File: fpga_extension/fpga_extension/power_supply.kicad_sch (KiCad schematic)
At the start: 3 parts, among them U1 AMS1117-1.2

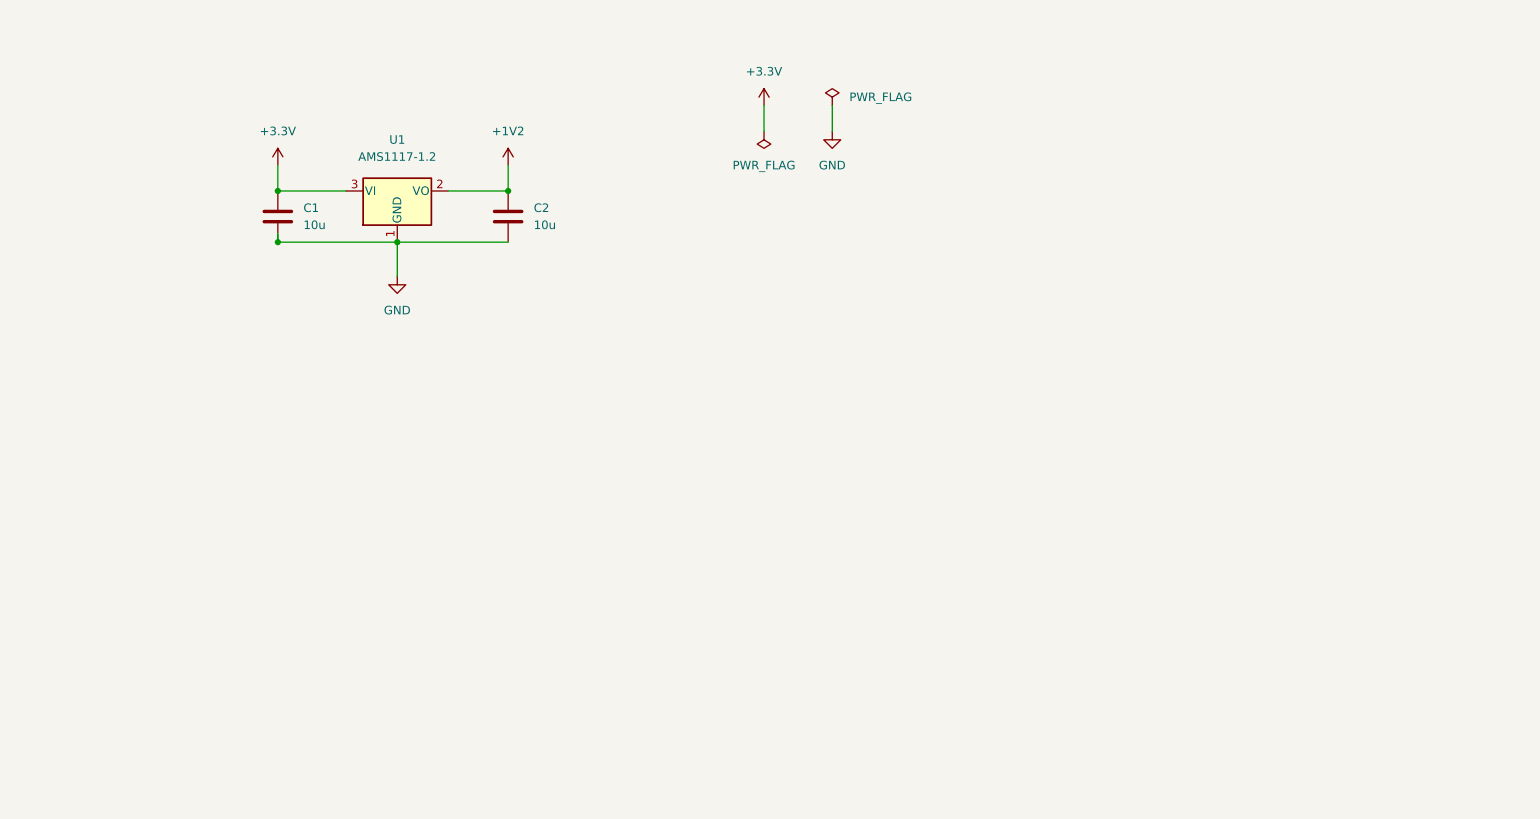
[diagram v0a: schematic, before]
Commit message: qspi added
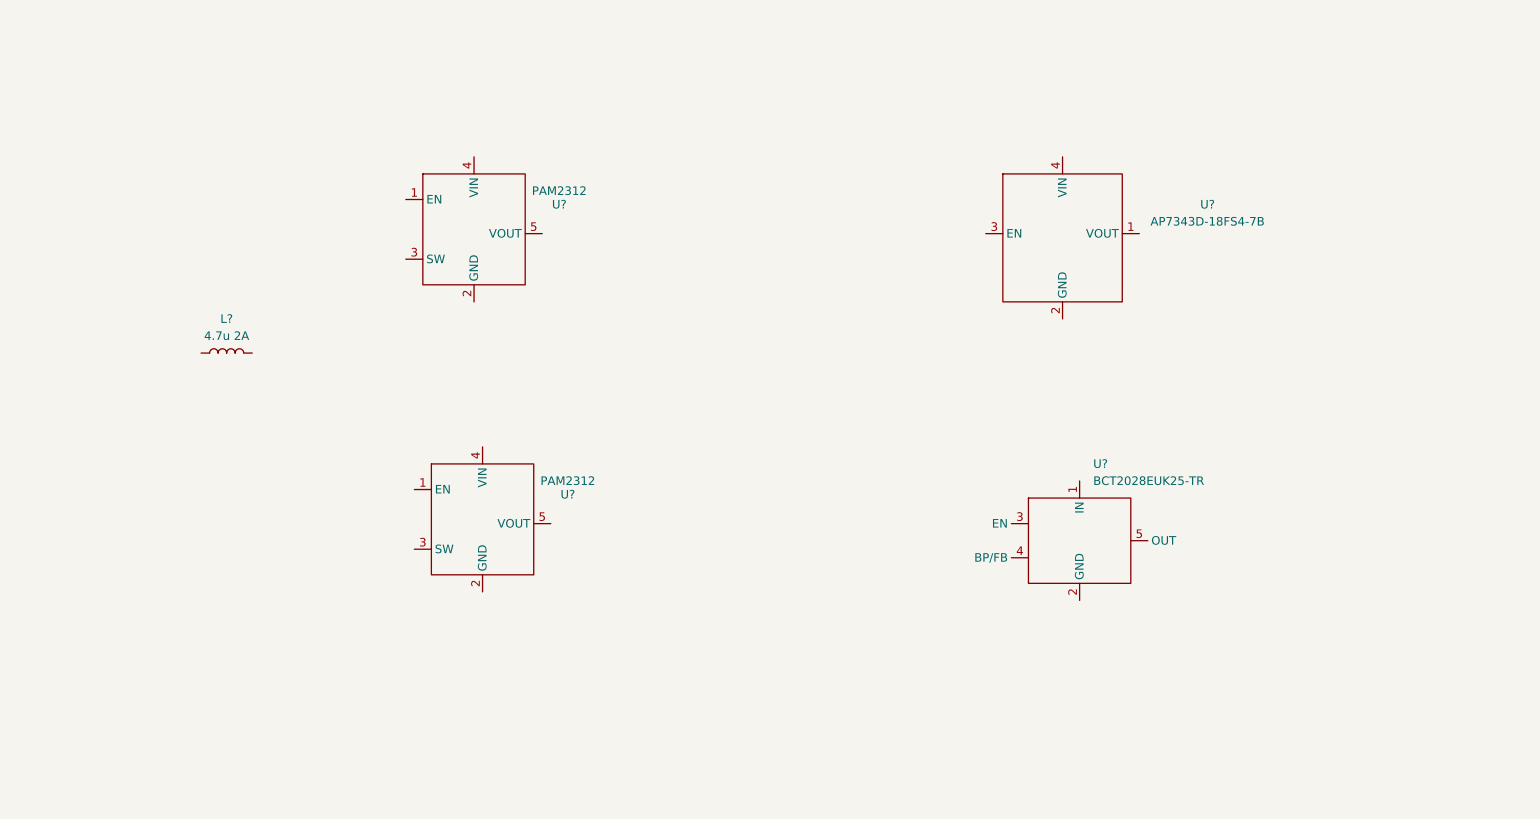
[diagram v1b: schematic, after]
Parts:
- removed C1, C2: 10u, Capacitor_SMD:C_0603_1608Metric_Pad1.08x0.95mm_HandSolder, symbol Device:C
- removed U1: AMS1117-1.2, Package_TO_SOT_SMD:SOT-223-3_TabPin2, symbol custom_ldo:AMS1117-1.2
- added L?: 4.7u 2A, fpga_extension:L_TDK_SLF6025, symbol Device:L
- added U? (x2): PAM2312, Package_TO_SOT_SMD:TSOT-23-5_HandSoldering, symbol fpga_extension_library:PAM2312
- added U?: BCT2028EUK25-TR, Package_TO_SOT_SMD:SOT-23-5_HandSoldering, symbol fpga_extension_library:BCT2028EUK25-TR
- added U?: AP7343D-18FS4-7B, fpga_extension:VREG_AP7340D-25FS4-7, symbol fpga_extension_library:AP7343D-18FS4-7B

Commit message: some ERC fixes
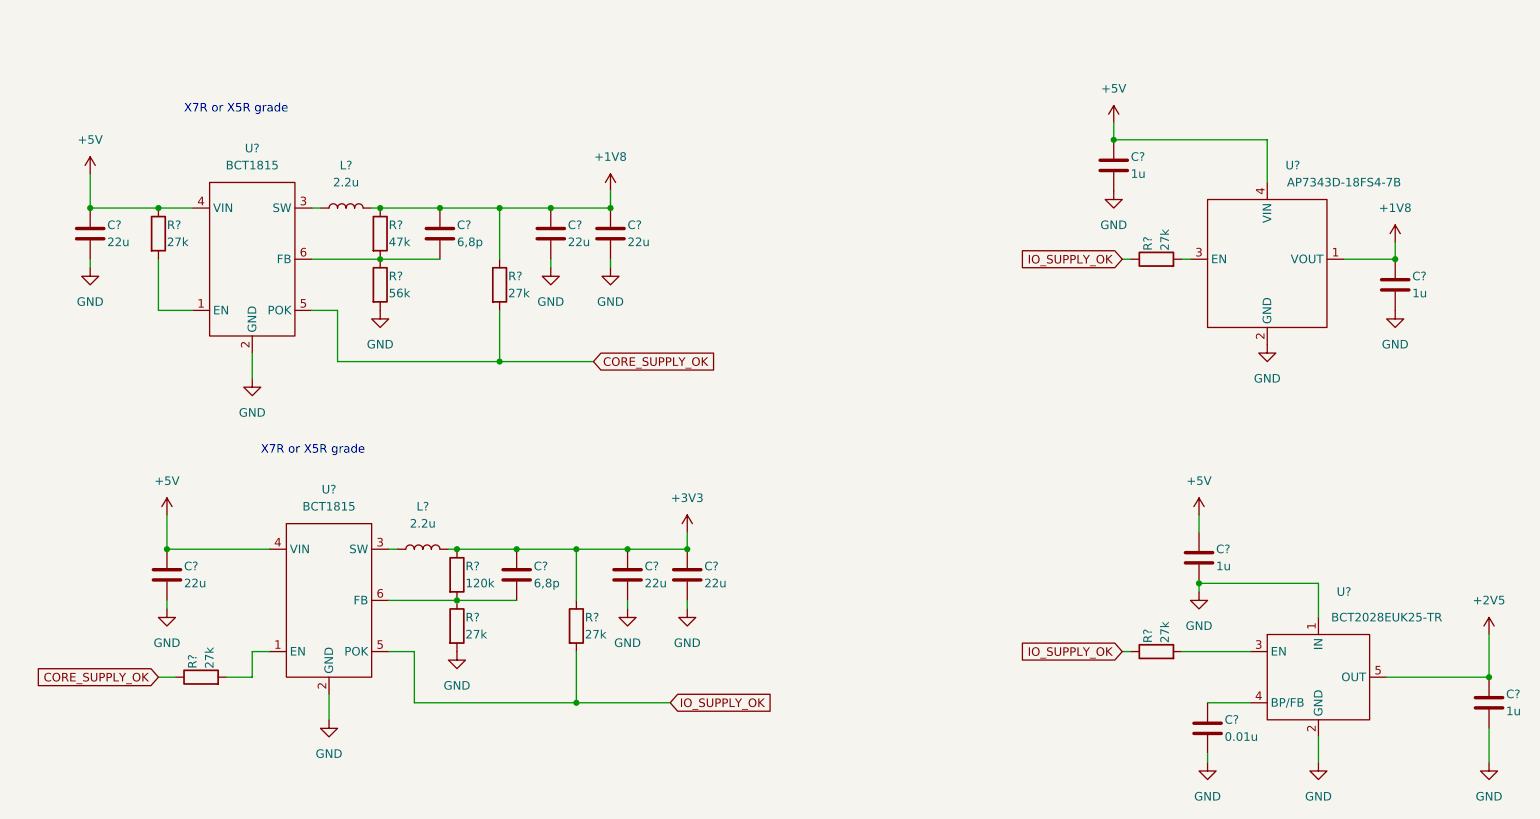
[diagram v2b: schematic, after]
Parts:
- removed L?: 4.7u 2A, fpga_extension:L_TDK_SLF6025, symbol Device:L
- removed U? (x2): PAM2312, Package_TO_SOT_SMD:TSOT-23-5_HandSoldering, symbol fpga_extension_library:PAM2312
- removed U?: BCT2028EUK25-TR, Package_TO_SOT_SMD:SOT-23-5_HandSoldering, symbol fpga_extension_library:BCT2028EUK25-TR
- added C? (x6): 22u, symbol Device:C
- added C? (x4): 1u, symbol Device:C
- added C? (x2): 6,8p, symbol Device:C
- added C?: 0.01u, symbol Device:C
- added L? (x2): 2.2u, symbol Device:L
- added R? (x7): 27k, symbol Device:R
- added R?: 120k, symbol Device:R
- added R?: 56k, symbol Device:R
- added R?: 47k, symbol Device:R
- added U? (x2): BCT1815, Package_TO_SOT_SMD:SOT-23-6_Handsoldering, symbol fpga_extension_library:BCT1815
- added U?: BCT2028EUK25-TR, Package_TO_SOT_SMD:SOT-23-5_HandSoldering, symbol fpga_extension_library:BCT2028EUK25-TR
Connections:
- net +1V8: now reaches U?.1 (VOUT)
- net +1V8: now also C?.1, C?.1, C?.1, C?.1, L?.2, R?.1, R?.1
- net GND: now reaches U?.2 (GND)
- net GND: now also C?.2, C?.2, C?.2, C?.2, C?.2, C?.2, C?.2, C?.2, C?.2, C?.2, C?.2, R?.2, R?.2, U?.1 (IN), U?.2 (GND), U?.2 (GND), U?.2 (GND)
- net at U?.3 (EN): now also R?.2
- net +5V: now reaches U?.4 (VIN)
- net +5V: now also C?.1, C?.1, C?.1, C?.1, R?.1, U?.4 (VIN), U?.4 (VIN)
- new net: R?.2, U?.1 (EN) (x2)
- new net: L?.1, U?.3 (SW) (x2)
- new net: C?.2, R?.1, R?.2, U?.6 (FB) (x2)
- new net: R?.2, U?.3 (EN)
- new net: C?.1, U?.4 (BP/FB)
- new net +2V5: C?.1, U?.5 (OUT)
- new net +3V3: C?.1, C?.1, C?.1, L?.2, R?.1, R?.1
- new net CORE_SUPPLY_OK: R?.1, R?.2, U?.5 (POK)
- new net IO_SUPPLY_OK: R?.1, R?.1, R?.2, U?.5 (POK)
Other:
- note added: "X7R or X5R grade"
- moved on the sheet: U?

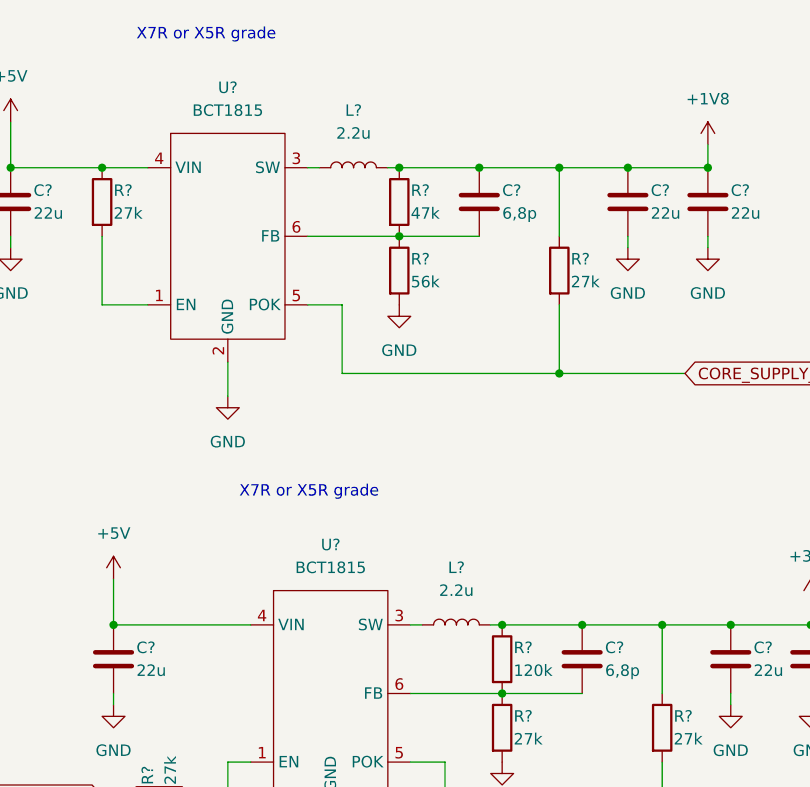
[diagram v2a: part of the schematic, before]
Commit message: gpu and motherboard passes tests, now time for fpga
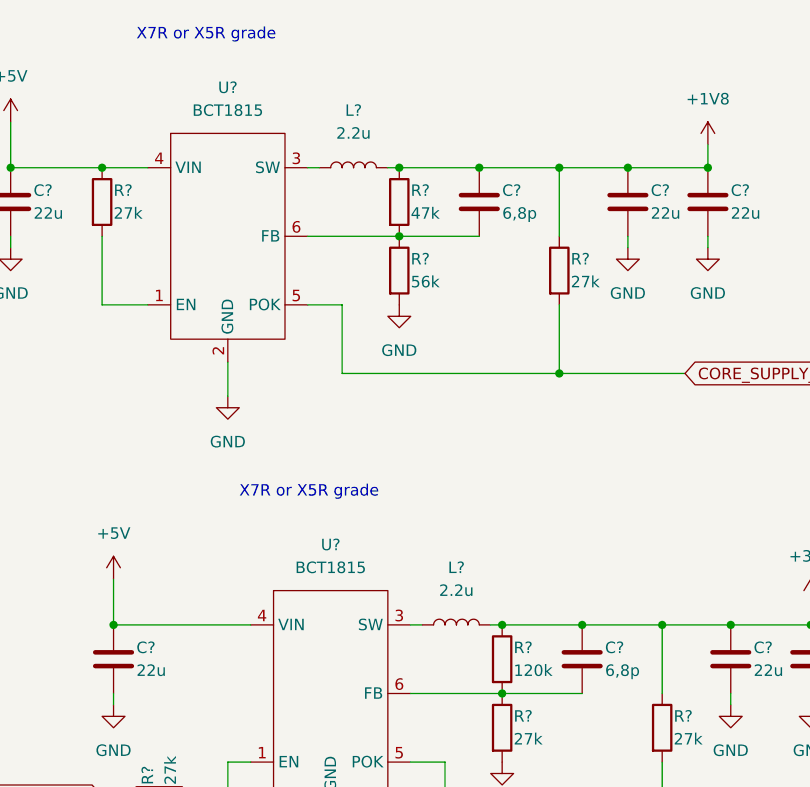
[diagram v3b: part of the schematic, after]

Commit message: refactored mainboard schematic
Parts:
- removed C? (x6): 22u, symbol Device:C
- removed C? (x4): 1u, symbol Device:C
- removed C? (x2): 6,8p, symbol Device:C
- removed C?: 0.01u, symbol Device:C
- removed L? (x2): 2.2u, symbol Device:L
- removed R? (x7): 27k, symbol Device:R
- removed R?: 120k, symbol Device:R
- removed R?: 56k, symbol Device:R
- removed R?: 47k, symbol Device:R
- removed U? (x2): BCT1815, Package_TO_SOT_SMD:SOT-23-6_Handsoldering, symbol fpga_extension_library:BCT1815
- removed U?: BCT2028EUK25-TR, Package_TO_SOT_SMD:SOT-23-5_HandSoldering, symbol fpga_extension_library:BCT2028EUK25-TR
- removed U?: AP7343D-18FS4-7B, fpga_extension:VREG_AP7340D-25FS4-7, symbol fpga_extension_library:AP7343D-18FS4-7B
- added C306, C308: 10u, Capacitor_SMD:C_0805_2012Metric_Pad1.18x1.45mm_HandSolder, symbol Device:C
- added C307: 4.7u, Capacitor_SMD:C_0805_2012Metric_Pad1.18x1.45mm_HandSolder, symbol Device:C
- added C310, C316: 100n, Capacitor_SMD:C_0603_1608Metric_Pad1.08x0.95mm_HandSolder, symbol Device:C
- added C313: 1u, Capacitor_SMD:C_0603_1608Metric_Pad1.08x0.95mm_HandSolder, symbol Device:C
- added C314: 3300p, Capacitor_SMD:C_0603_1608Metric_Pad1.08x0.95mm_HandSolder, symbol Device:C
- added C317, C319: 22u, Capacitor_SMD:C_0603_1608Metric_Pad1.08x0.95mm_HandSolder, symbol Device:C
- added C318: 22p, Capacitor_SMD:C_0603_1608Metric_Pad1.08x0.95mm_HandSolder, symbol Device:C
- added C320, C322: 22u, Capacitor_SMD:C_0805_2012Metric_Pad1.18x1.45mm_HandSolder, symbol Device:C
- added L302: 3.3u, footprints:NRS8030, symbol Device:L
- added L303: 2.2u, footprints:NRS8030, symbol Device:L
- added R304: 120k, Resistor_SMD:R_0603_1608Metric_Pad0.98x0.95mm_HandSolder, symbol Device:R
- added R305: 3.3k, Resistor_SMD:R_0603_1608Metric_Pad0.98x0.95mm_HandSolder, symbol Device:R
- added R306: 22k, Resistor_SMD:R_0603_1608Metric_Pad0.98x0.95mm_HandSolder, symbol Device:R
- added R307: 200k, Resistor_SMD:R_0603_1608Metric_Pad0.98x0.95mm_HandSolder, symbol Device:R
- added R308: 100k, Resistor_SMD:R_0603_1608Metric_Pad0.98x0.95mm_HandSolder, symbol Device:R
- added TP306: TestPoint, TestPoint:TestPoint_Pad_D1.5mm, symbol Connector:TestPoint
- added U304: BD9D321EFJ, footprints:SOIC127P600X100-9N, symbol project_power:BD9D321EFJ
- added U5: TLV62569APDRLR, footprints:SOT50P160X60-6N, symbol project_power:TLV62569APDRLR
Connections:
- net +5V: now also C307.1, C318.1, C320.1, C322.1, L302.2, R304.1, TP306.1, U5.3 (VIN), U5.5 (EN)
- net GND: now also C306.2, C307.2, C308.2, C310.2, C313.2, C314.2, C317.2, C320.2, C322.2, R306.2, R308.2, U304.5 (GND), U304.9 (FIN), U5.2 (GND)
- new net: C318.2, R305.2, R306.1, U304.2 (FB)
- new net: C316.1, U304.7 (BOOT)
- new net: C316.2, L302.1, U304.6 (SW)
- new net: C313.1, U304.3 (VREG)
- new net: R307.2, R308.1, U5.1 (FB)
- new net: L303.1, U5.4 (SW)
- new net: C317.1, C319.1, L303.2, R307.1
- new net: C314.1, U304.4 (SS)
- new net: R304.2, R305.1
- new net VDC: C306.1, C308.1, C310.1, U304.1 (EN), U304.8 (VIN)
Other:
- note added: "Power section 5V bus"
- note removed: "X7R or X5R grade"
